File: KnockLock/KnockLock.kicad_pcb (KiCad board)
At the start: 2 copper layers, 90 x 60 mm, 51 parts, among them IC1 ESP32-C3-WROOM-02-N4, IC2 LM2575-3.3WT, J1 Screw_Terminal_01x02, J2 USB3145-30-1-A, J3 TBP04R12-500-03BE, J4 UART, J5 Boot Pins, Q1 IRLML6402TRPBF, Q2 BC547B

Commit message: Started routing
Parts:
- removed J4: UART, Connector_PinHeader_2.54mm:PinHeader_1x02_P2.54mm_Vertical
- turned Q1 to 180 degrees
- renumbered AccSens to U1
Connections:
- IC1 pad 10: unconnected-(IC1-IO10-Pad10) -> BUZZ
- IC1 pad 6: BUZZ -> unconnected-(IC1-IO7-Pad6)
- J2 pad 2: unconnected-(J2-Pad2) -> TX
- J2 pad 3: unconnected-(J2-Pad3) -> RX
- J2 pad 4: unconnected-(J2-Pad4) -> GND
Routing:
- net +5V: track 0.00 -> 57.1 mm
- net +3.3V: track 16.9 -> 49.7 mm
- net BAT_V: track 0.00 -> 24.9 mm
- net Net-(D7-K): track 0.00 -> 20.1 mm
- net BUZZ: track 0.00 -> 18.5 mm
- net +3V3: track 0.00 -> 13.8 mm
- net Net-(F2-Pad1): track 0.00 -> 12.8 mm
- net Net-(J1-Pin_1): track 0.00 -> 9.45 mm

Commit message: return to direct uart
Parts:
- added J4: UART, Connector_PinHeader_2.54mm:PinHeader_1x02_P2.54mm_Vertical, F.Cu at (81.8, 85.2)
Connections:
- J2 pad 2: TX -> unconnected-(J2-Pad2)
- J2 pad 3: RX -> unconnected-(J2-Pad3)
- J2 pad 4: GND -> unconnected-(J2-Pad4)
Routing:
- net TX: track 0.00 -> 6.23 mm
- net RX: track 0.00 -> 5.80 mm

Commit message: First draft of routing complete, parts list updated, 3d models added, button changed
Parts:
- removed S1: 2-1977223-8, 2-1977223-8:219772238
- added S2: TS02-66-60-BK-260-LCR-D, TS02-66-60-BK-260-LCR-D:SW_TS02-66-60-BK-260-LCR-D, F.Cu at (48.8, 89.3)
- moved R3 1.86 mm to (79.6, 80.8)
- moved R4 0.66 mm to (79.7, 76.3)
- moved R5 0.60 mm to (79.7, 71.8)
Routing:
- net +5V: track 57.1 -> 144.6 mm
- net GND: track 0.00 -> 79.8 mm, vias 0 -> 1
- net Net-(D1-K): track 0.00 -> 61.0 mm
- net CONTROL: track 0.00 -> 48.1 mm
- net SDA: track 0.00 -> 47.1 mm, vias 0 -> 2
- net SCL: track 0.00 -> 46.6 mm, vias 0 -> 2
- net +3.3V: track 49.7 -> 92.2 mm, vias 0 -> 1
- net WAKE_INT: track 0.00 -> 38.1 mm, vias 0 -> 4
- net MRESET: track 0.00 -> 31.7 mm
- net BAT_V: track 24.9 -> 50.9 mm, vias 0 -> 1
- net SERVO: track 0.00 -> 23.7 mm, vias 0 -> 1
- net Net-(Q1-G): track 0.00 -> 20.4 mm
- net Net-(IC1-IO8): track 0.00 -> 19.8 mm, vias 0 -> 1
- net Net-(Q2-B): track 0.00 -> 17.8 mm
- net +3V3: track 13.8 -> 31.0 mm
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- added copper zone on F.Cu, net GND

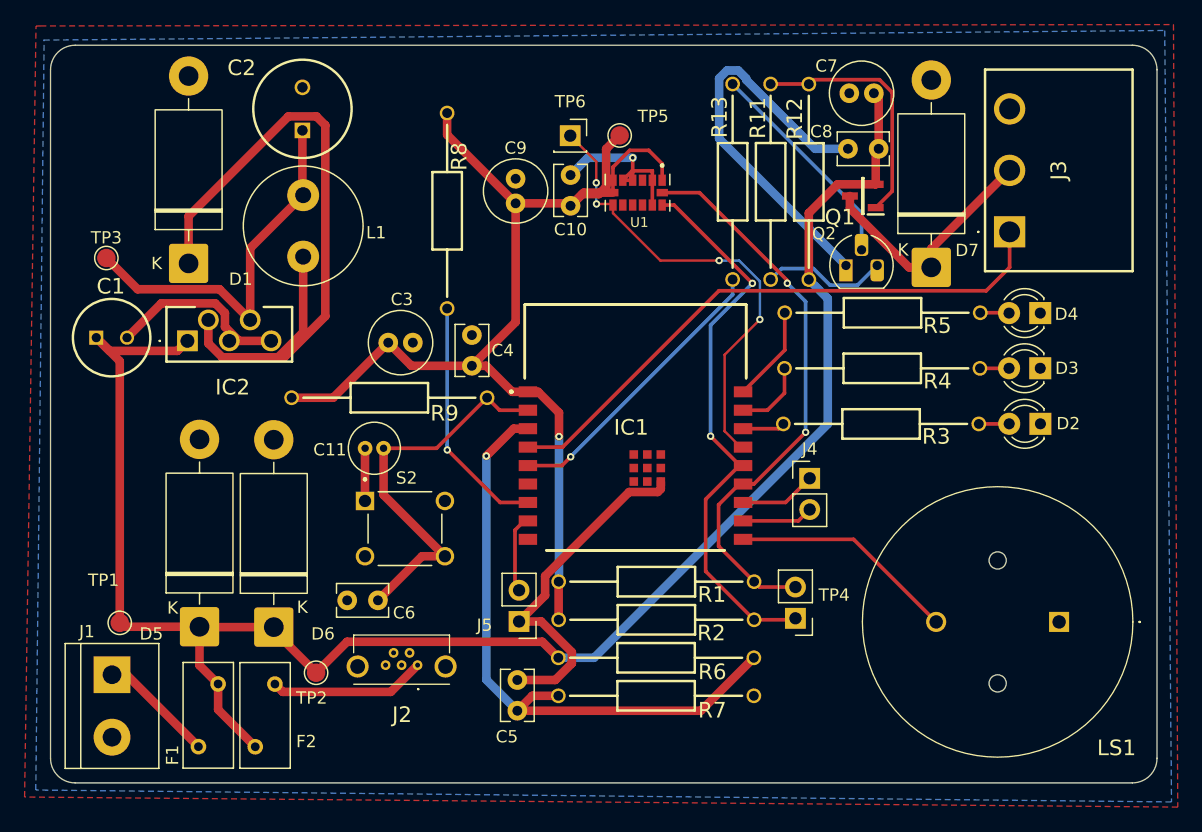
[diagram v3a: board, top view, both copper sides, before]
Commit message: Updates to PCB Dft
- I added some labels on the silkscreen for the boot and UART pins
- Cleaned up the voltage regulator circuit
- Made sure everything connets to the ground plane
    - added some GND vias
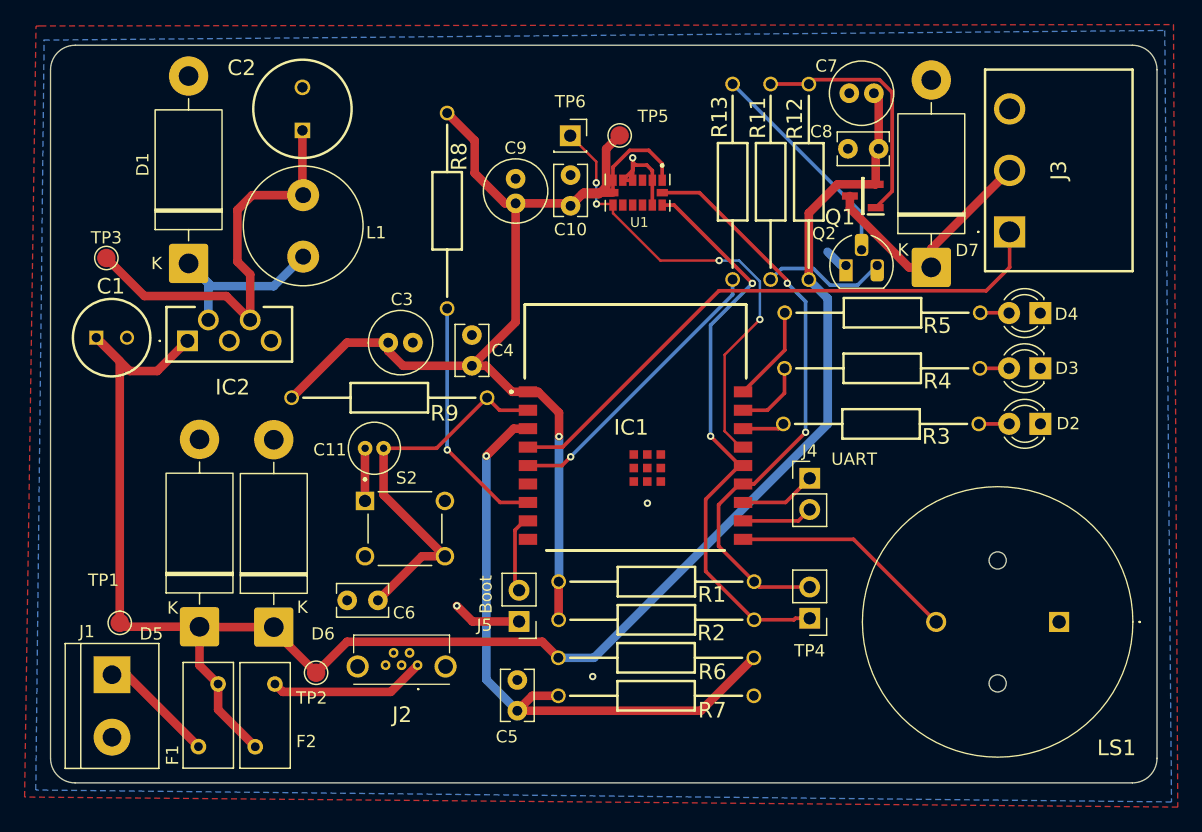
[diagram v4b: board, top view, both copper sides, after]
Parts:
- moved TP4 1.16 mm to (81.8, 96.6)
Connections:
- C1 pad 2: Net-(C1--) -> GND
- IC1 pad 19: unconnected-(IC1-GND_2-Pad19) -> GND
- IC1 pad 20: unconnected-(IC1-GND_3-Pad20) -> GND
- IC1 pad 21: unconnected-(IC1-GND_4-Pad21) -> GND
- IC1 pad 22: unconnected-(IC1-GND_5-Pad22) -> GND
- IC1 pad 23: unconnected-(IC1-GND_6-Pad23) -> GND
- IC1 pad 24: unconnected-(IC1-GND_7-Pad24) -> GND
- IC1 pad 25: unconnected-(IC1-GND_8-Pad25) -> GND
- IC1 pad 26: unconnected-(IC1-GND_9-Pad26) -> GND
- IC2 pad 3: Net-(C1--) -> GND
- IC2 pad 5: Net-(C1--) -> GND
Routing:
- net GND: track 79.8 -> 20.6 mm, vias 1 -> 4
- net Net-(D1-K): track 61.0 -> 16.3 mm
- net Net-(C1--): track 14.8 -> 0.00 mm
- net +3V3: track 31.0 -> 34.5 mm
- net +5V: track 144.6 -> 146.0 mm
- net SDA: track 47.1 -> 48.3 mm
- net SCL: track 46.6 -> 47.8 mm
- net +3.3V: track 92.2 -> 93.1 mm
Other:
- board text added: "Boot"
- board text added: "UART"
